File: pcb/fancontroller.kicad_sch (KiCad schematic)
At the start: 41 parts, among them J1 Thermo, J2 USB_C_PC, J3 SWD, SW1 NRST, SW2 BOOT0, U1 STM32F103C8Tx, U2 XC6206PxxxMR, U3 TPS5430DDA, U4 USBLC6-2SC6, Y1 16MHz

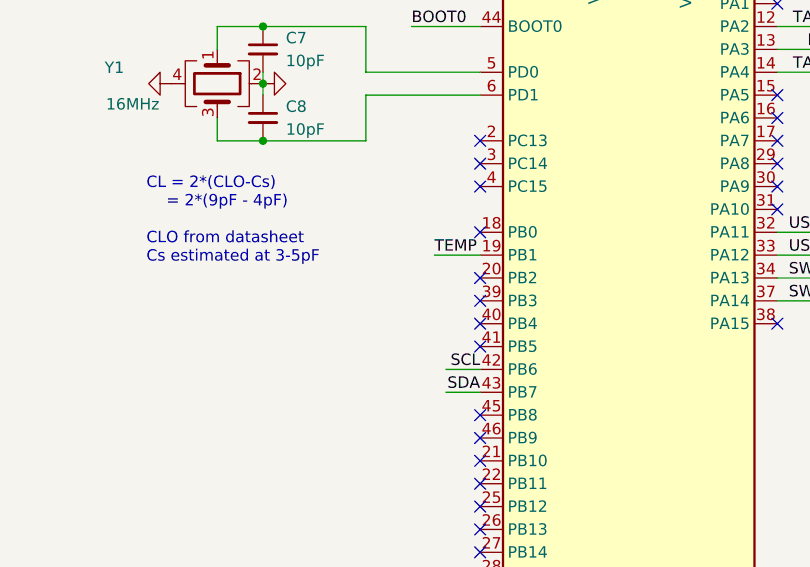
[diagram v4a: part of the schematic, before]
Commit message: add app led, commit attempts to use 0.91" display
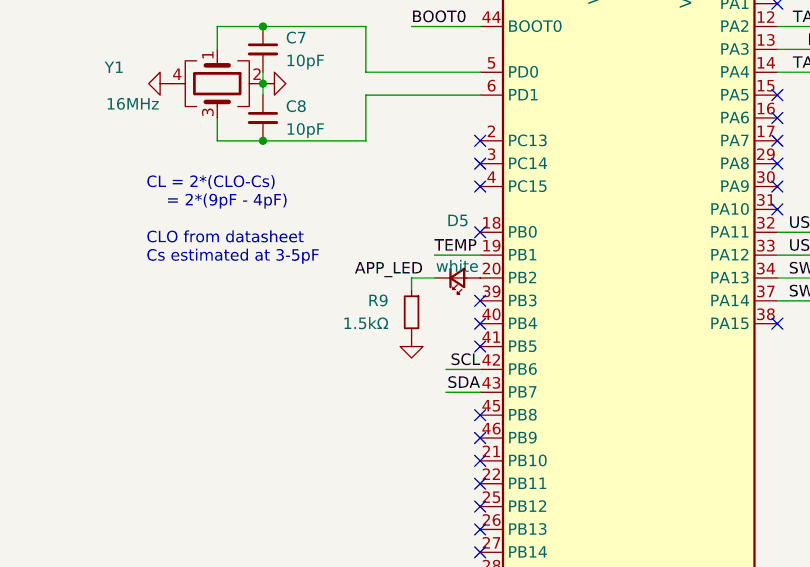
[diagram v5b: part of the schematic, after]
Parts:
- added D5: white, LED_SMD:LED_0603_1608Metric, symbol Device:LED_Small
- added R9: 1.5kΩ, Resistor_SMD:R_0402_1005Metric, symbol Device:R_Small
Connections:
- net GND: now also R9.2
- net at U1.20 (PB2): now also D5.2 (A)
- new net APP_LED: D5.1 (K), R9.1
- no-connect marks 29 -> 28
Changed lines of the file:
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@@
 		(at 140.97 113.03)
 	)
-	(no_connect
-		(at 107.95 130.81)
-	)
 	(wire
 		(pts
@@
 		)
 	)
+	(wire
+		(pts
+			(xy 102.87 130.81) (xy 100.33 130.81)
+		)
+		(stroke
+			(width 0)
+			(type default)
+		)
+	)
 	(polyline
 		(pts
@@
 	(wire
 		(pts
+			(xy 100.33 130.81) (xy 100.33 132.08)
+		)
+		(stroke
+			(width 0)
+			(type default)
+		)
+	)
+	(wire
+		(pts
 			(xy 204.47 68.58) (xy 196.85 68.58)
 		)
@@
 		)
 	)
+	(label "APP_LED"
+		(at 101.6 130.81 180)
+		(fields_autoplaced yes)
+		(effects
+			(font
+				(size 1.27 1.27)
+			)
+			(justify right bottom)
+		)
+	)
 	(label "PWM"
 		(at 148.59 105.41 180)
@@
 	)
 	(symbol
+		(lib_id "power:GND")
+		(at 100.33 137.16 0)
+		(unit 1)
+		(exclude_from_sim no)
+		(in_bom yes)
+		(on_board yes)
+		(dnp no)
+		(fields_autoplaced yes)
+		(property "Reference" "#PWR09"
+			(at 100.33 143.51 0)
+			(effects
+				(font
+					(size 1.27 1.27)
+				)
+				(hide yes)
+			)
+		)
+		(property "Value" "GND"
+			(at 100.33 142.24 0)
+			(effects
+				(font
+					(size 1.27 1.27)
+				)
+				(hide yes)
+			)
+		)
+		(property "Footprint" ""
+			(at 100.33 137.16 0)
+			(effects
+				(font
+					(size 1.27 1.27)
+				)
+				(hide yes)
+			)
+		)
+		(property "Datasheet" ""
+			(at 100.33 137.16 0)
+			(effects
+				(font
+					(size 1.27 1.27)
+				)
+				(hide yes)
+			)
+		)
+		(property "Description" "Power symbol creates a global label with name \"GND\" , ground"
+			(at 100.33 137.16 0)
+			(effects
+				(font
+					(size 1.27 1.27)
+				)
+				(hide yes)
+			)
+		)
+		(pin "1"
+		)
+		(instances
+			(project "fancontroller"
+				(path "/0fbc55e3-1cb3-420e-a547-fc7bb589a137"
+					(reference "#PWR09")
+					(unit 1)
+				)
+			)
+		)
+	)
+	(symbol
 		(lib_id "power:+3.3VA")
 		(at 130.81 92.71 0)
@@
 	)
 	(symbol
+		(lib_id "Device:R_Small")
+		(at 100.33 134.62 0)
+		(mirror y)
+		(unit 1)
+		(exclude_from_sim no)
+		(in_bom yes)
+		(on_board yes)
+		(dnp no)
+		(fields_autoplaced yes)
+		(property "Reference" "R9"
+			(at 97.79 133.35 0)
+			(effects
+				(font
+					(size 1.27 1.27)
+				)
+				(justify left)
+			)
+		)
+		(property "Value" "1.5kΩ"
+			(at 97.79 135.89 0)
+			(effects
+				(font
+					(size 1.27 1.27)
+				)
+				(justify left)
+			)
+		)
+		(property "Footprint" "Resistor_SMD:R_0402_1005Metric"
+			(at 100.33 134.62 0)
+			(effects
+				(font
+					(size 1.27 1.27)
+				)
+				(hide yes)
+			)
+		)
+		(property "Datasheet" "~"
+			(at 100.33 134.62 0)
+			(effects
+				(font
+					(size 1.27 1.27)
+				)
+				(hide yes)
+			)
+		)
+		(property "Description" ""
+			(at 100.33 134.62 0)
+			(effects
+				(font
+					(size 1.27 1.27)
+				)
+				(hide yes)
+			)
+		)
+		(pin "2"
+		)
+		(pin "1"
+		)
+		(instances
+			(project "fancontroller"
+				(path "/0fbc55e3-1cb3-420e-a547-fc7bb589a137"
+					(reference "R9")
+					(unit 1)
+				)
+			)
+		)
+	)
+	(symbol
 		(lib_id "power:GND")
 		(at 271.78 124.46 0)
@@
 					(unit 1)
 				)
+			)
+		)
+	)
+	(symbol
+		(lib_id "Device:LED_Small")
+		(at 105.41 130.81 0)
+		(mirror x)
+		(unit 1)
+		(exclude_from_sim no)
+		(in_bom yes)
+		(on_board yes)
+		(dnp no)
+		(property "Reference" "D5"
+			(at 105.4735 124.46 0)
+			(effects
+				(font
+					(size 1.27 1.27)
+				)
+			)
+		)
+		(property "Value" "white"
+			(at 105.41 129.54 0)
+			(effects
+				(font
+					(size 1.27 1.27)
+				)
+			)
+		)
+		(property "Footprint" "LED_SMD:LED_0603_1608Metric"
+			(at 105.41 130.81 90)
+			(effects
+				(font
+					(size 1.27 1.27)
+				)
+				(hide yes)
+			)
+		)
+		(property "Datasheet" "~"
+			(at 105.41 130.81 90)
+			(effects
+				(font
+					(size 1.27 1.27)
+				)
+				(hide yes)
+			)
+		)
+		(property "Description" ""
+			(at 105.41 130.81 0)
+			(effects
+				(font
+					(size 1.27 1.27)
+				)
+				(hide yes)
+			)
+		)
+		(pin "1"
+		)
+		(pin "2"
+		)
+		(instances
+			(project "fancontroller"
+				(path "/0fbc55e3-1cb3-420e-a547-fc7bb589a137"
+					(reference "D5")
+					(unit 1)
+				)

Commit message: Add LED
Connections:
- net at D5.2 (A): now also U1.28 (PB15); no longer U1.20 (PB2)
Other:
- moved on the sheet: D5, R9
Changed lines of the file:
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@@
 	)
 	(no_connect
+		(at 107.95 130.81)
+	)
+	(no_connect
 		(at 247.65 49.53)
 	)
@@
 	)
 	(no_connect
-		(at 107.95 163.83)
-	)
-	(no_connect
 		(at 107.95 133.35)
 	)
@@
 		)
 	)
+	(wire
+		(pts
+			(xy 100.33 163.83) (xy 100.33 165.1)
+		)
+		(stroke
+			(width 0)
+			(type default)
+		)
+	)
 	(polyline
 		(pts
@@
 	(wire
 		(pts
-			(xy 102.87 130.81) (xy 100.33 130.81)
+			(xy 102.87 163.83) (xy 100.33 163.83)
 		)
 		(stroke
@@
 	(wire
 		(pts
-			(xy 100.33 130.81) (xy 100.33 132.08)
-		)
-		(stroke
-			(width 0)
-			(type default)
-		)
-	)
-	(wire
-		(pts
 			(xy 204.47 68.58) (xy 196.85 68.58)
 		)
@@
 	)
 	(label "APP_LED"
-		(at 101.6 130.81 180)
+		(at 101.6 163.83 180)
 		(fields_autoplaced yes)
 		(effects
@@
 	(symbol
 		(lib_id "power:GND")
-		(at 100.33 137.16 0)
+		(at 100.33 170.18 0)
 		(unit 1)
 		(exclude_from_sim no)
@@
 		(fields_autoplaced yes)
 		(property "Reference" "#PWR09"
-			(at 100.33 143.51 0)
+			(at 100.33 176.53 0)
 			(effects
 				(font
@@
 		)
 		(property "Value" "GND"
-			(at 100.33 142.24 0)
+			(at 100.33 175.26 0)
 			(effects
 				(font
@@
 		)
 		(property "Footprint" ""
-			(at 100.33 137.16 0)
+			(at 100.33 170.18 0)
 			(effects
 				(font
@@
 		)
 		(property "Datasheet" ""
-			(at 100.33 137.16 0)
+			(at 100.33 170.18 0)
 			(effects
 				(font
@@
 		)
 		(property "Description" "Power symbol creates a global label with name \"GND\" , ground"
-			(at 100.33 137.16 0)
+			(at 100.33 170.18 0)
 			(effects
 				(font
@@
 	(symbol
 		(lib_id "Device:R_Small")
-		(at 100.33 134.62 0)
+		(at 100.33 167.64 0)
 		(mirror y)
 		(unit 1)
@@
 		(fields_autoplaced yes)
 		(property "Reference" "R9"
-			(at 97.79 133.35 0)
+			(at 97.79 166.37 0)
 			(effects
 				(font
@@
 		)
 		(property "Value" "1.5kΩ"
-			(at 97.79 135.89 0)
+			(at 97.79 168.91 0)
 			(effects
 				(font
@@
 		)
 		(property "Footprint" "Resistor_SMD:R_0402_1005Metric"
-			(at 100.33 134.62 0)
+			(at 100.33 167.64 0)
 			(effects
 				(font
@@
 		)
 		(property "Datasheet" "~"
-			(at 100.33 134.62 0)
+			(at 100.33 167.64 0)
 			(effects
 				(font
@@
 		)
 		(property "Description" ""
-			(at 100.33 134.62 0)
+			(at 100.33 167.64 0)
 			(effects
 				(font
@@
 	(symbol
 		(lib_id "Device:LED_Small")
-		(at 105.41 130.81 0)
+		(at 105.41 163.83 0)
 		(mirror x)
 		(unit 1)
@@
 		(dnp no)
 		(property "Reference" "D5"
-			(at 105.4735 124.46 0)
+			(at 105.4735 157.48 0)
 			(effects
 				(font
@@
 		)
 		(property "Value" "white"
-			(at 105.41 129.54 0)
+			(at 105.664 166.624 0)
 			(effects
 				(font
@@
 		)
 		(property "Footprint" "LED_SMD:LED_0603_1608Metric"
-			(at 105.41 130.81 90)
+			(at 105.41 163.83 90)
 			(effects
 				(font
@@
 		)
 		(property "Datasheet" "~"
-			(at 105.41 130.81 90)
+			(at 105.41 163.83 90)
 			(effects
 				(font
@@
 		)
 		(property "Description" ""
-			(at 105.41 130.81 0)
+			(at 105.41 163.83 0)
 			(effects
 				(font

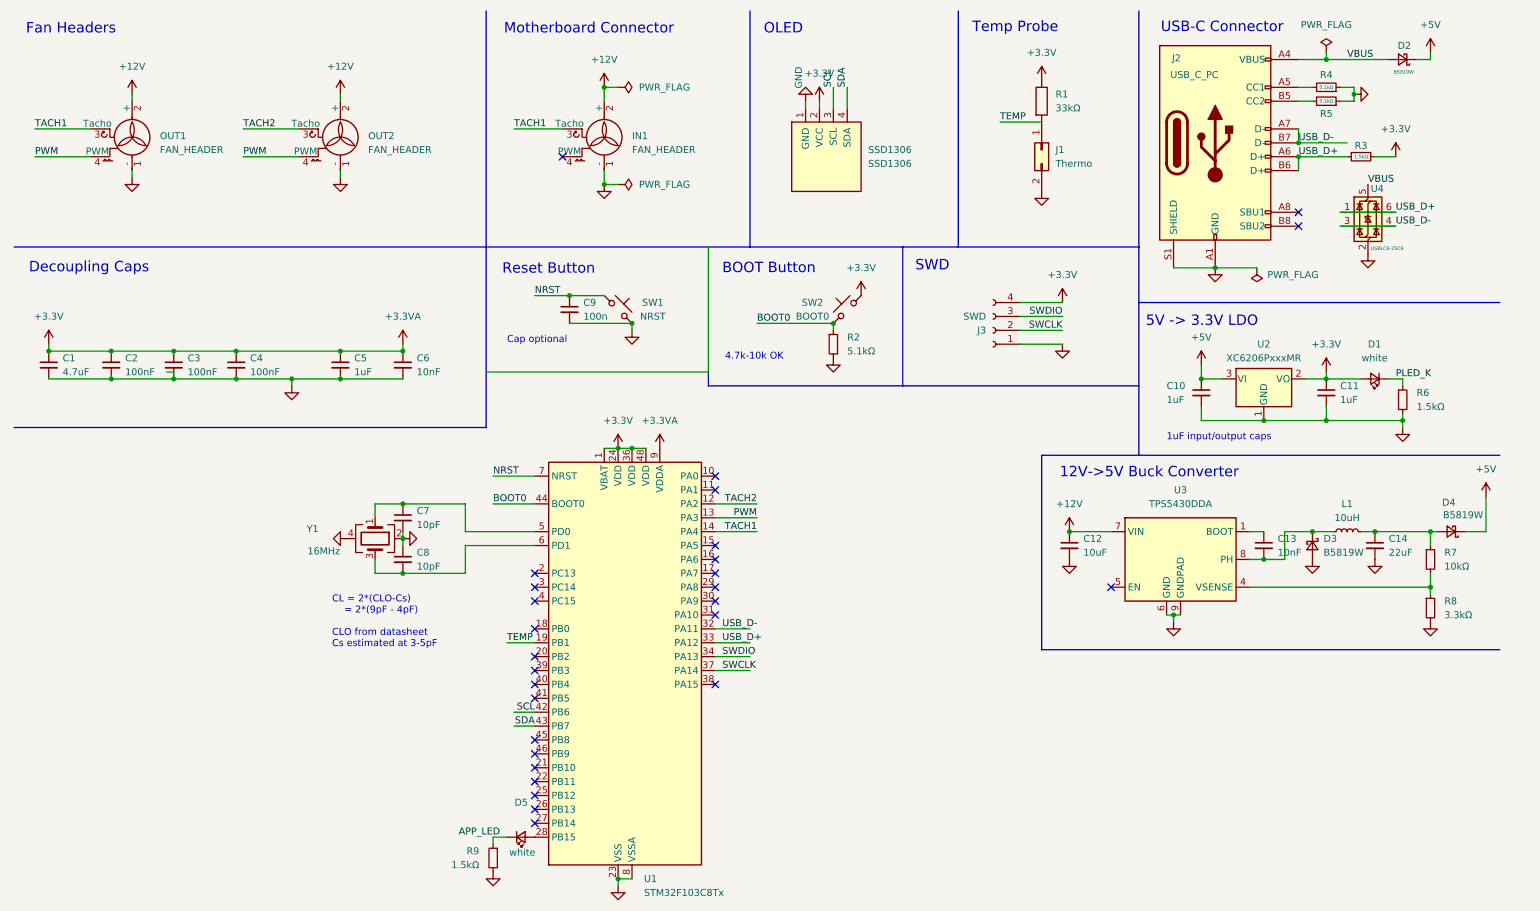
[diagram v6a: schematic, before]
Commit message: Begin rev3: drop USB connector, plan for OLED mounting
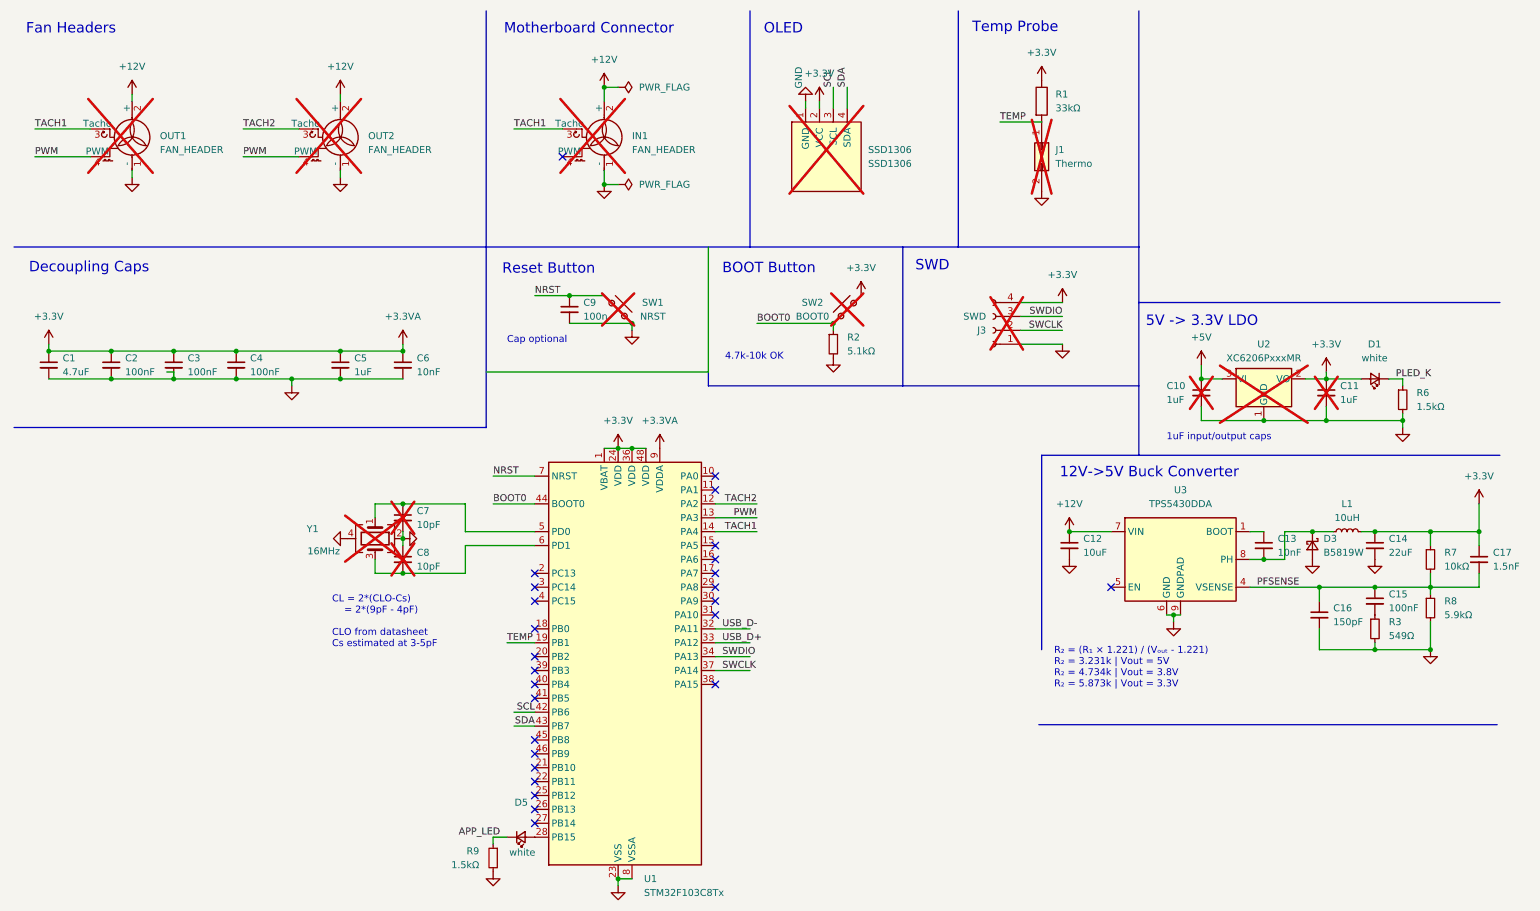
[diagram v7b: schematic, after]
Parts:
- removed D2, D4: B5819W, Diode_SMD:D_SOD-123, symbol Device:D_Schottky_Small
- removed J2: USB_C_PC, Connector_USB:USB_C_Receptacle_XKB_U262-16XN-4BVC11, symbol Connector:USB_C_Receptacle_USB2.0_16P
- removed R4, R5: 5.1kΩ, Resistor_SMD:R_0402_1005Metric, symbol Device:R_Small
- removed U4: USBLC6-2SC6, Package_TO_SOT_SMD:SOT-23-6, symbol Power_Protection:USBLC6-2SC6
- added C15: 100nF, Capacitor_SMD:C_0402_1005Metric, symbol Device:C_Small
- added C16: 150pF, Capacitor_SMD:C_0603_1608Metric, symbol Device:C_Small
- added C17: 1.5nF, Capacitor_SMD:C_0603_1608Metric, symbol Device:C_Small
- C10, C11, C7, C8, IN1, J1, OUT1, OUT2, SSD1306, SW1, SW2, U2, Y1: now not fitted; now left out of the parts list
- J3: now not fitted
- R3: value 1.5kΩ -> 549Ω; footprint Resistor_SMD:R_0402_1005Metric -> Resistor_SMD:R_0603_1608Metric
- R8: value 3.3kΩ -> 5.9kΩ; footprint Resistor_SMD:R_0402_1005Metric -> Resistor_SMD:R_0603_1608Metric
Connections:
- net +3.3V: now also C14.1, L1.2, R7.1, C17.1; no longer R3.2
- net GND: now also R3.2, C16.2
- net USB_D+: no longer R3.1
- net PFSENSE: now reaches R7.2, R8.1, U3.4 (VSENSE)
- net PFSENSE: now also C15.1, C16.1, C17.2
- new net: C15.2, R3.1
- no-connect marks 28 -> 26
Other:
- note added: "R₂ = (R₁ × 1.221) / (Vₒᵤₜ - 1.221) R₂ = 3.231k | Vout = 5V R₂ = 4.734k | Vout = 3.8V R₂ = 5.873k | Vout = 3.3V"
- note removed: "USB-C Connector"
